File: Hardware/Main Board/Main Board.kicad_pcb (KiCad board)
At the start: 4 copper layers, 70 x 48 mm, 67 parts, among them J1 Micro_SD_Card_Det1, J2 Camera Module, J3 Conn_01x09_Socket, J4 MIC 1 Connector, J5 MIC 2 Connector, J6 USB_C_Receptacle_USB2.0_16P, J7 OLED, Q1 AO3401A, U1 ESP32-S3-WROOM-2, U2 TPS63060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

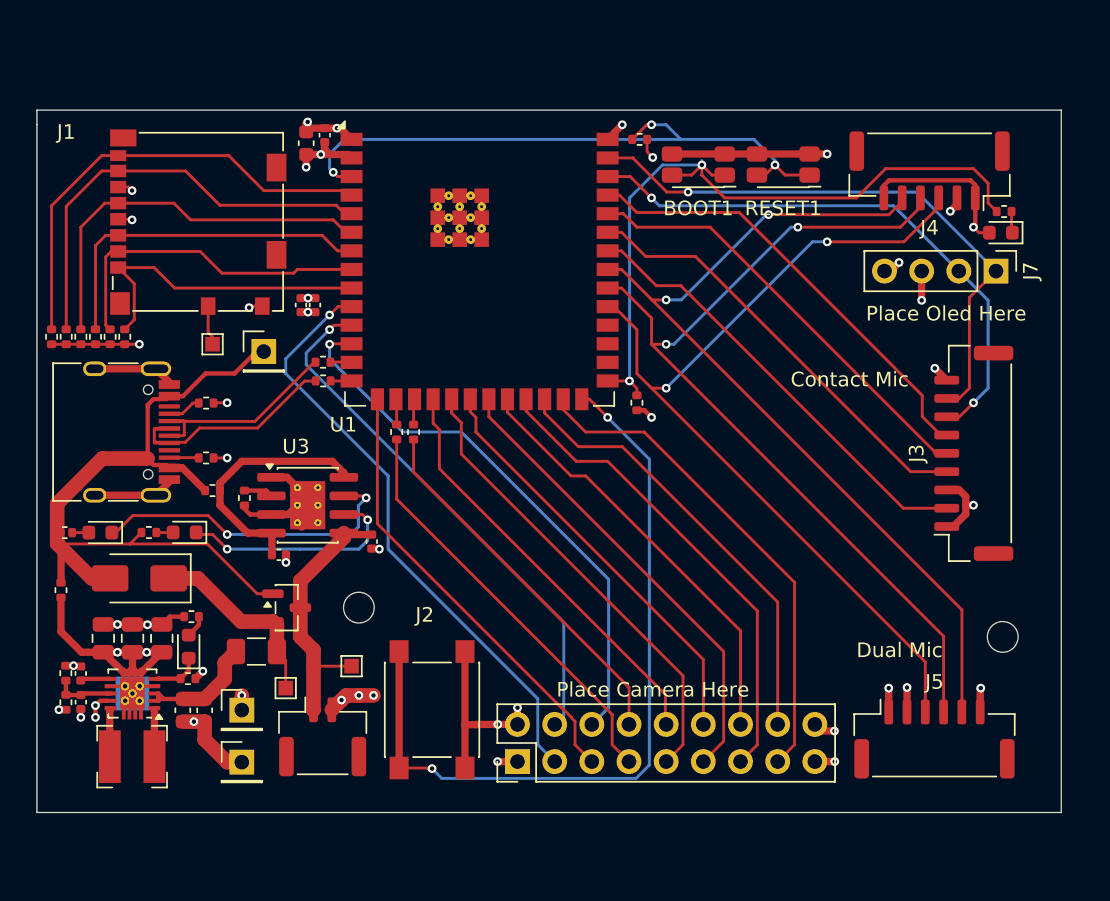
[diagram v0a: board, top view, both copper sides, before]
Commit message: received feedback from Andy + others and revised board
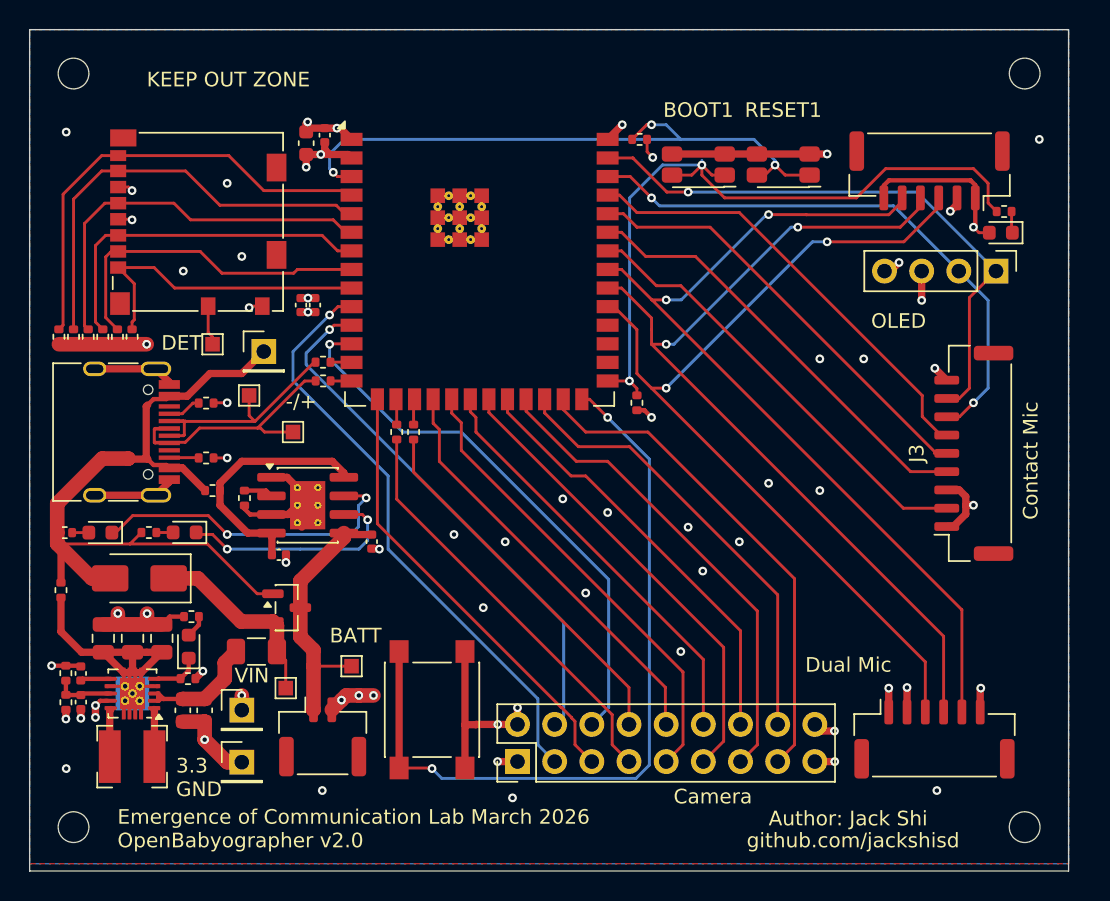
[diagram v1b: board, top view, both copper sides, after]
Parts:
- added H3: MountingHole, MountingHole:MountingHole_2.1mm, F.Cu at (76.5, 45.5)
- added H4: MountingHole, MountingHole:MountingHole_2.1mm, F.Cu at (141.5, 45.5)
- added TP7: TestPoint, TestPoint:TestPoint_Pad_1.0x1.0mm, F.Cu at (91.5, 70.0)
- added TP8: TestPoint, TestPoint:TestPoint_Pad_1.0x1.0mm, F.Cu at (88.5, 67.5)
- moved H1 24.6 mm to (76.5, 97.0)
- moved H2 13.1 mm to (141.5, 97.0)
- moved R2 0.50 mm to (76.5, 63.5)
- moved R3 0.50 mm to (80.5, 63.5)
- moved R4 0.50 mm to (77.5, 63.5)
- moved R5 0.50 mm to (79.5, 63.5)
- moved R6 0.50 mm to (75.5, 63.5)
- moved R7 0.50 mm to (78.5, 63.5)
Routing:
- net /D+: track 18.1 -> 20.6 mm
- net /D-: track 14.7 -> 16.6 mm
- net +3.3V: track 43.3 -> 45.0 mm
- net GND: track 95.3 -> 96.9 mm, vias 27 -> 48
- net +5V_USB: track 52.2 -> 52.8 mm
- added copper zone on B.Cu, net GND
- added copper zone on F.Cu, net GND
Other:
- board size 70 x 48 mm -> 71 x 57.5 mm
- board text added: "-/+"
- board text added: "3.3 GND"
- board text added: "Author: Jack Shi"
- board text added: "BATT"
- board text added: "Camera"
- board text added: "DET"
- board text added: "Emergence of Communication Lab March 2026 OpenBabyographer v2.0"
- board text added: "KEEP OUT ZONE"
- board text added: "OLED"
- board text added: "VIN"
- board text added: "github.com/jackshisd"
- board text removed: "Place Camera Here"
- board text removed: "Place Oled Here"

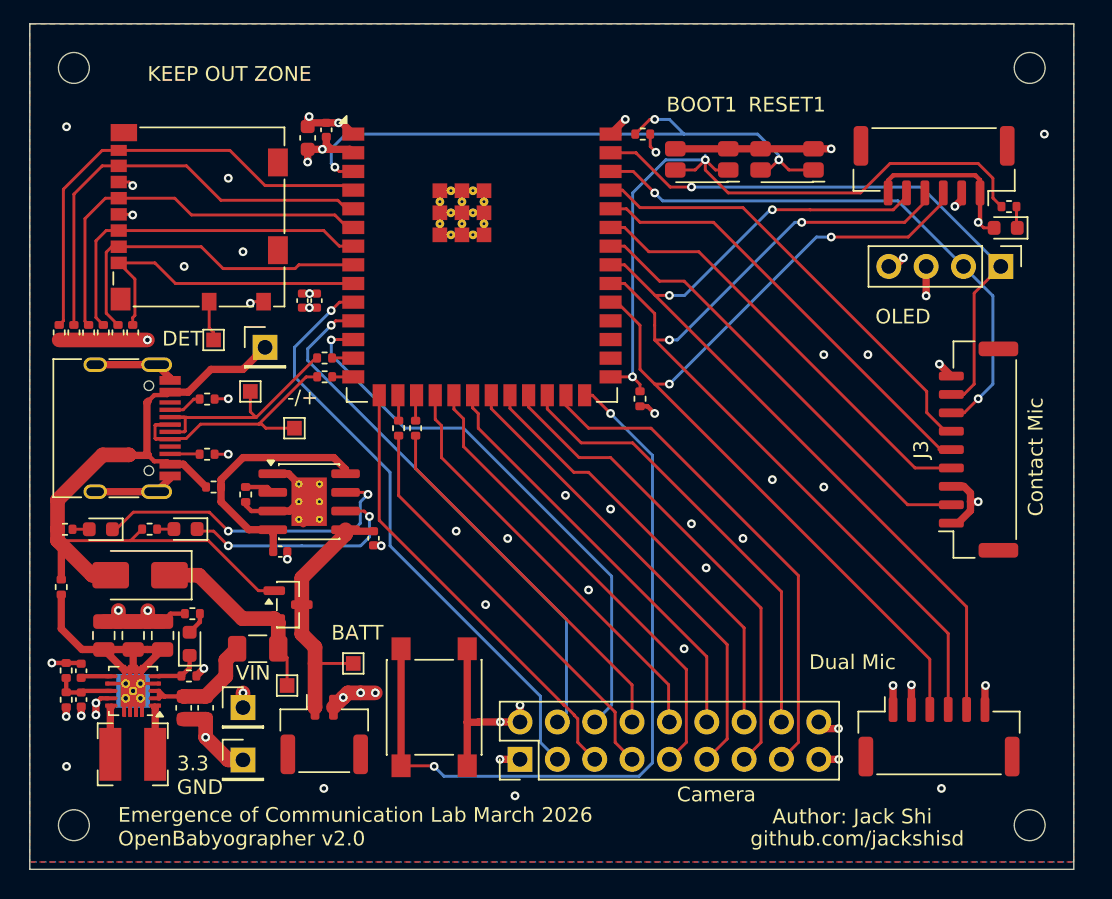
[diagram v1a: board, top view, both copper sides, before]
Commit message: submitted for manufacturinng. Flipped contact mic connections on main board to be aligned with contact mic board
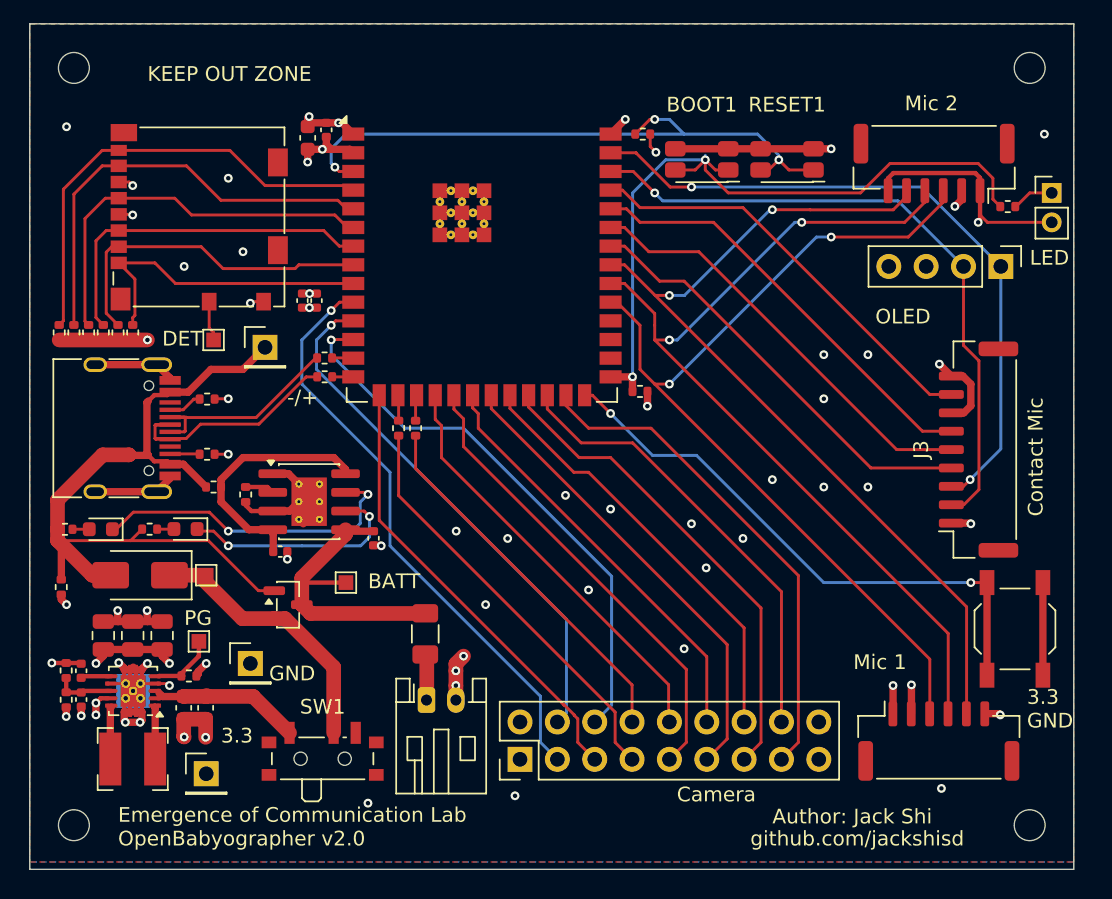
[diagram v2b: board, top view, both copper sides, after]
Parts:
- removed D4: LED, LED_SMD:LED_0603_1608Metric
- removed R20: 1k, Resistor_SMD:R_0402_1005Metric
- removed TP7, TP8: TestPoint, TestPoint:TestPoint_Pad_1.0x1.0mm
- added SW1: SW_SPST, Button_Switch_SMD:SW_SPDT_PCM12, F.Cu at (93.4, 92.1)
- added TP9: TestPoint, TestPoint:TestPoint_Pad_1.0x1.0mm, F.Cu at (85.0, 84.5)
- BT1: footprint Connector_JST:JST_GH_SM02B-GHS-TB_1x02-1MP_P1.25mm_Horizontal -> Connector_JST:JST_PH_S2B-PH-K_1x02_P2.00mm_Horizontal
- D1: footprint LED_SMD:LED_0603_1608Metric -> Connector_PinHeader_2.00mm:PinHeader_1x02_P2.00mm_Vertical
- USER_INPUT1: footprint Button_Switch_SMD:SW_SPST_PTS645 -> Button_Switch_SMD:SW_SPST_TL3342
- moved USER_INPUT1 39.9 mm to (140.5, 83.7)
- moved F1 11.4 mm to (100.4, 84.0), turned to -90 degrees
- moved TP4 9.30 mm to (85.5, 80.0)
- moved BT1 7.34 mm to (100.5, 88.5)
- moved TP1 6.58 mm to (88.5, 86.0)
- moved TP5 5.52 mm to (95.0, 80.5)
- moved TP2 5.15 mm to (85.5, 93.5)
- moved D1 3.93 mm to (143.0, 54.0), turned to 0 degrees
- moved R12 0.50 mm to (115.0, 67.5), turned to 180 degrees
- moved L1 0.32 mm to (80.5, 92.5)
- moved J5 0.30 mm to (135.3, 91.3)
- moved J4 0.15 mm to (135.0, 52.0)
- moved R11 0.08 mm to (140.0, 54.9)
- turned C11 to -90 degrees
- turned C12 to -90 degrees
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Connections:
- BT1 pad 1: +BATT -> Net-(BT1-+)
- C5 pad 2: Net-(U2-EN) -> Net-(SW1-A)
- C6 pad 2: Net-(U2-EN) -> Net-(SW1-A)
- F1 pad 1: VIN -> +BATT
- F1 pad 2: Net-(U2-EN) -> Net-(BT1-+)
- J3 pad 1: GND -> +3.3V
- J3 pad 2: CONTACT_SCLK -> I2C_SCL
- J3 pad 3: GND -> I2C_SDA
- J3 pad 4: CONTACT_LRCK -> CONTACT_MCLK
- J3 pad 6: CONTACT_MCLK -> CONTACT_LRCK
- J3 pad 7: I2C_SCL -> GND
- J3 pad 8: I2C_SDA -> CONTACT_SCLK
- J3 pad 9: +3.3V -> GND
- U1 pad 34: CONTACT_SCLK -> CONTACT_MCLK
- U1 pad 35: CONTACT_LRCK -> CONTACT_ASDOUT
- U1 pad 36: CONTACT_ASDOUT -> CONTACT_LRCK
- U1 pad 37: CONTACT_MCLK -> CONTACT_SCLK
- U2 pad 2: Net-(U2-EN) -> Net-(SW1-A)
- U2 pad 3: Net-(U2-EN) -> Net-(SW1-A)
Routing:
- net Net-(U1-IO45): track 52.9 -> 38.9 mm
- net GND: track 96.9 -> 84.1 mm, vias 48 -> 54
- net Net-(SW1-A): track 0.00 -> 10.6 mm
- net Net-(U2-EN): track 8.38 -> 0.00 mm
- net I2C_SDA: track 41.0 -> 47.2 mm, vias 1 -> 2
- net I2C_SCL: track 39.7 -> 45.6 mm, vias 2 -> 1
- net VIN: track 13.3 -> 18.2 mm
- net Net-(BT1-+): track 0.00 -> 3.15 mm
- net /D+: track 20.6 -> 18.1 mm
- net /D-: track 16.6 -> 14.7 mm
- net +BATT: track 18.3 -> 20.1 mm
- net Net-(D4-A): track 1.55 -> 0.00 mm
- net CONTACT_SCLK: track 30.5 -> 28.9 mm
- net Net-(D1-K): track 1.47 -> 2.86 mm
- net CONTACT_MCLK: track 30.8 -> 29.4 mm
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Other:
- board text added: "3.3"
- board text added: "Emergence of Communication Lab OpenBabyographer v2.0"
- board text added: "GND"
- board text added: "LED"
- board text added: "Mic 1"
- board text added: "Mic 2"
- board text added: "PG"
- board text removed: "Dual Mic"
- board text removed: "Emergence of Communication Lab March 2026 OpenBabyographer v2.0"
- board text removed: "VIN"

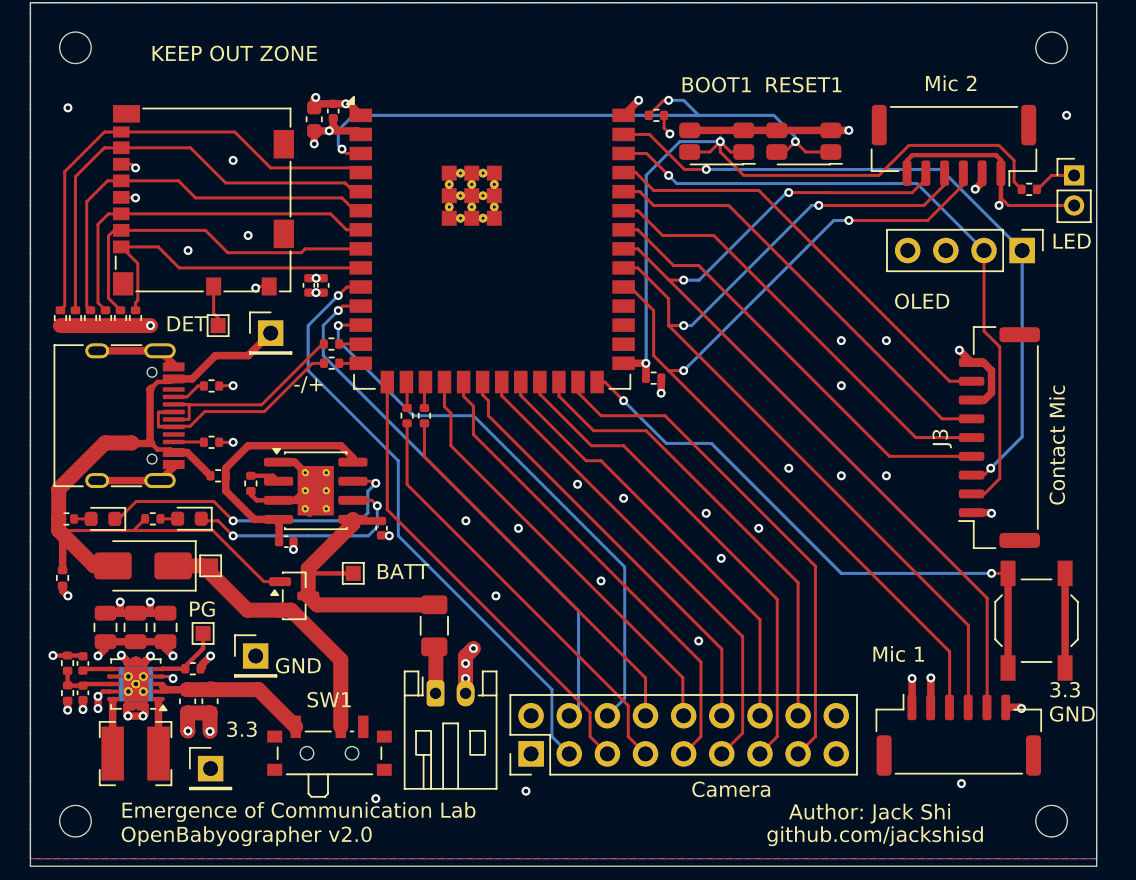
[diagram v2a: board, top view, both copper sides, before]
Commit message: fixed power button and via proximity to pad on main board
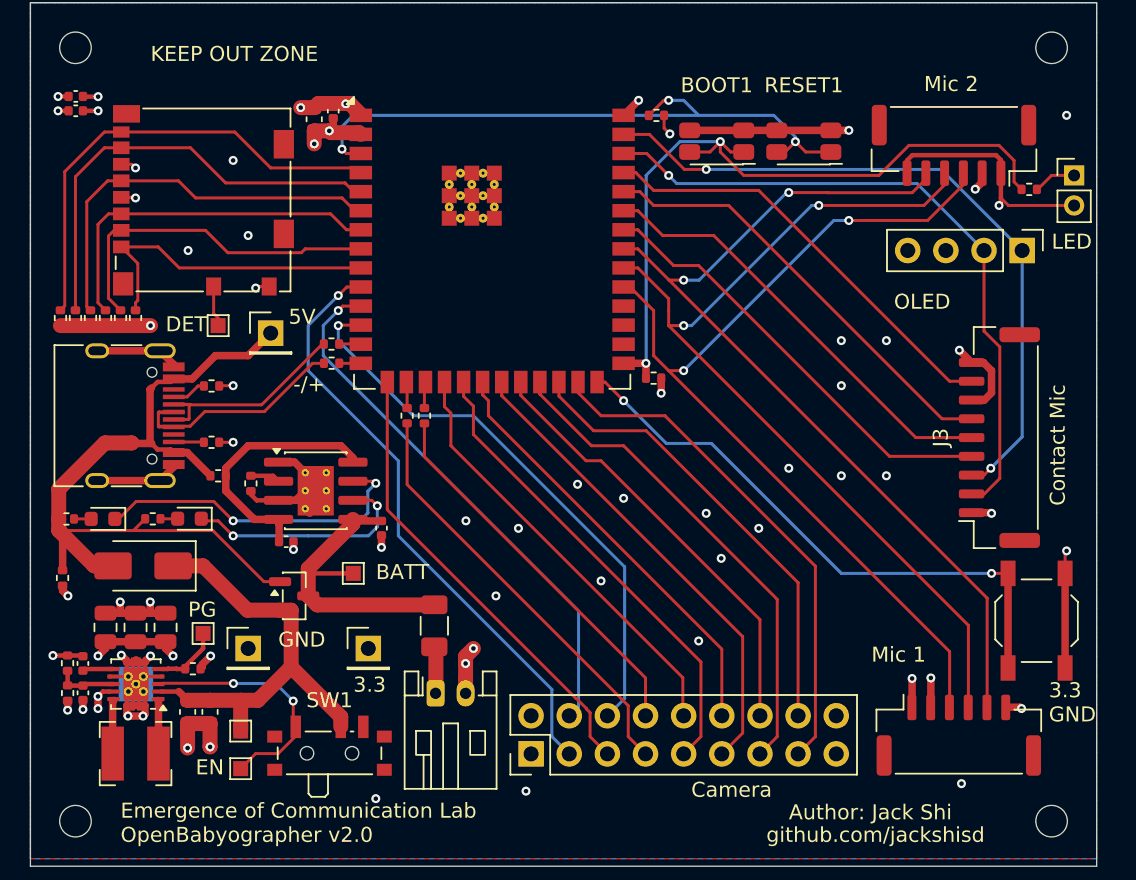
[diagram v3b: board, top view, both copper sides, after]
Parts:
- added TP7: TestPoint, TestPoint:TestPoint_Pad_1.0x1.0mm, F.Cu at (87.5, 93.5)
- moved C2 20.2 mm to (76.5, 49.7), turned to 180 degrees
- moved C1 20.0 mm to (76.5, 48.7), turned to 180 degrees
- moved TP2 13.2 mm to (96.0, 85.5)
- moved TP4 11.2 mm to (87.5, 91.0)
- moved C5 0.71 mm to (84.0, 89.7)
- moved C6 0.71 mm to (85.5, 89.7)
- moved TP1 0.71 mm to (88.0, 85.5)
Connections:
- C5 pad 2: Net-(SW1-A) -> VIN
- C6 pad 2: Net-(SW1-A) -> VIN
- U2 pad 2: Net-(SW1-A) -> VIN
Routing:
- net VIN: track 18.2 -> 30.0 mm
- net Net-(SW1-A): track 10.6 -> 16.2 mm, vias 0 -> 2
- net GND: track 84.1 -> 87.0 mm, vias 54 -> 53
- net +3.3V: track 43.9 -> 45.8 mm, vias 16 -> 17
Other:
- board text added: "5V"
- board text added: "EN"
